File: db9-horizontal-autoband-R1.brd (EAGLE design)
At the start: 33 x 37 mm, 19 parts, among them U8 PCA9536

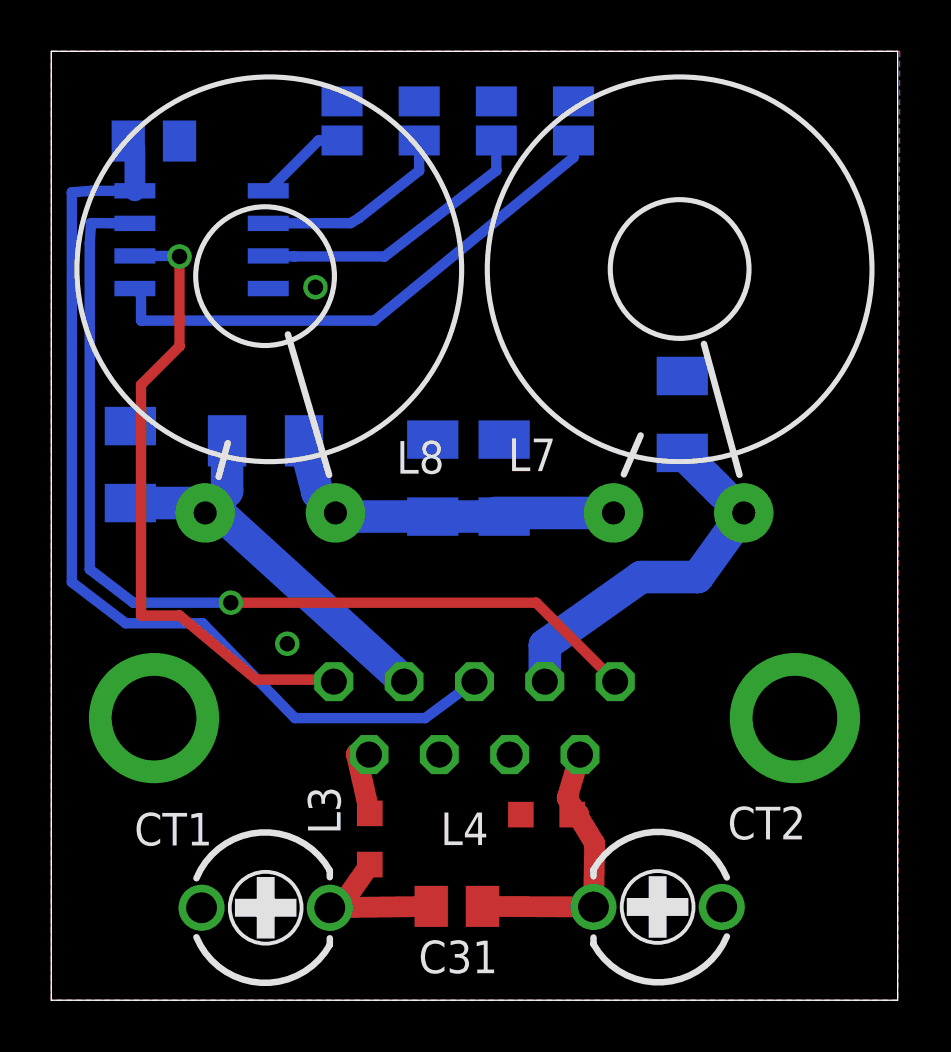
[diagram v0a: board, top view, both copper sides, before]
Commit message: Fixed errors on horizontal autoband module
Errors fixed:
- Disconnected DB9 pin 7 to allow for future use
- Added 1mm holes to allow toroids to be tied down
- Moved solder jumpers to make room forholes
- Fixed board title text so that it will actually print
- Adjusted restrict on board edge to be narrower
- Minor text placement fixes
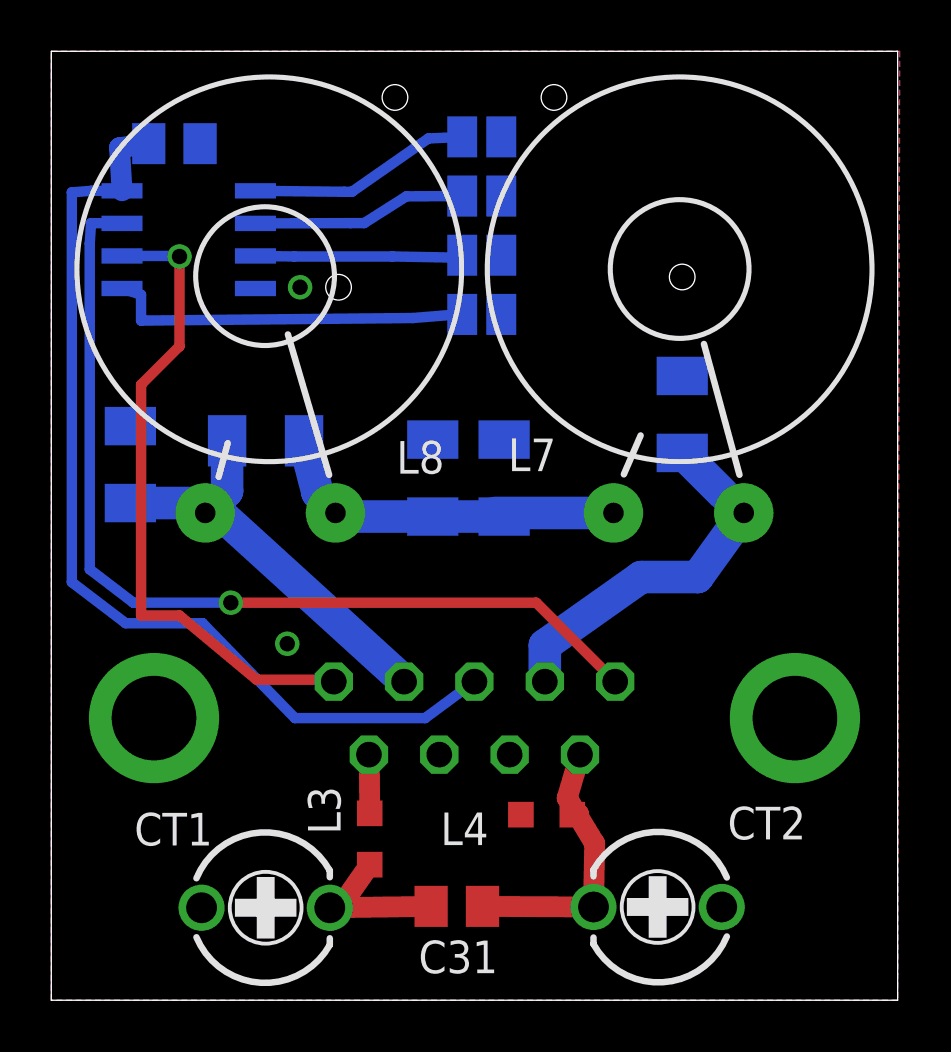
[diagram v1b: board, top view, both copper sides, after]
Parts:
- moved 3 8.35 mm to (16.8, 26.7), turned to 180 degrees
- moved 0 5.48 mm to (16.8, 33.7), turned to 180 degrees
- moved 2 5.27 mm to (16.8, 29.0), turned to 180 degrees
- moved 1 3.81 mm to (16.8, 31.4), turned to 180 degrees
- moved C100 0.81 mm to (4.80, 33.4)
- moved U8 0.50 mm to (5.36, 29.7)
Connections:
- net GND: no longer X1.7
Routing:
- net N$10: track 21.1 -> 14.4 mm
- net N$13: track 3.69 -> 8.72 mm
- net N$11: track 11.2 -> 8.11 mm
- net N$12: track 7.76 -> 8.37 mm
